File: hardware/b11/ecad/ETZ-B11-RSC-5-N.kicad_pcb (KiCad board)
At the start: 2 copper layers, 112.3 x 85.8 mm, 36 parts, among them SW1 MX-Hotswap-1U, SW10 MX-Hotswap-1U, SW11 MX-Hotswap-1U, SW12 MX-Hotswap-1U, SW13 MX-Hotswap-1U, SW14 MX-Hotswap-1U, SW15 MX-Hotswap-1U, SW16 MX-Hotswap-1U, SW17 MX-Hotswap-1U, SW18 MX-Hotswap-1U, SW2 MX-Hotswap-1U, SW3 MX-Hotswap-1U, SW4 MX-Hotswap-1U, SW5 MX-Hotswap-1U, SW6 MX-Hotswap-1U, SW7 MX-Hotswap-1U, SW8 MX-Hotswap-1U, SW9 MX-Hotswap-1U

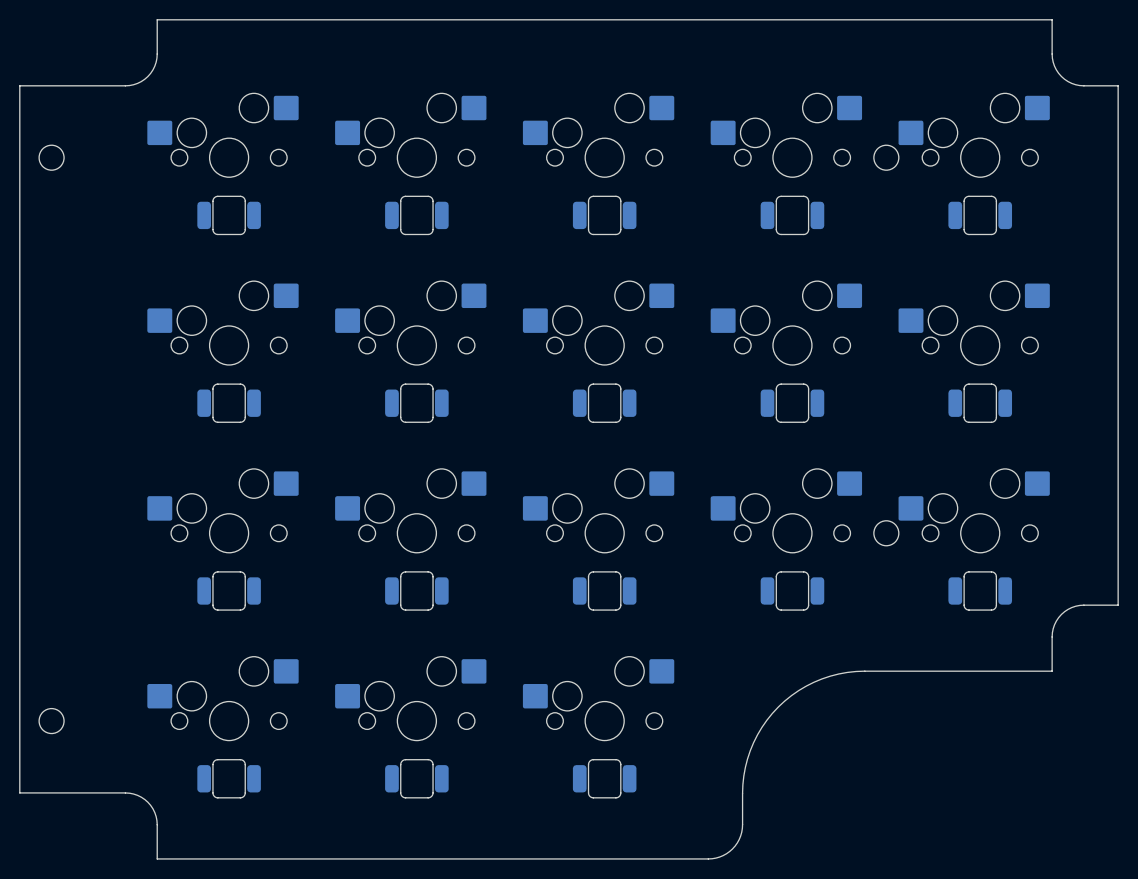
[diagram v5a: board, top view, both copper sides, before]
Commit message: fix(hardware/b11): adjust LED offset to 5.0mm and regenerate all carrier PCBs
Reduces south-facing LED offset from 5.9mm to 5.0mm (closer to the
standard 5.08mm switch-to-LED spacing). All 8 carrier PCBs regenerated.

Co-Authored-By: Claude Sonnet 4.6 <noreply@anthropic.com>
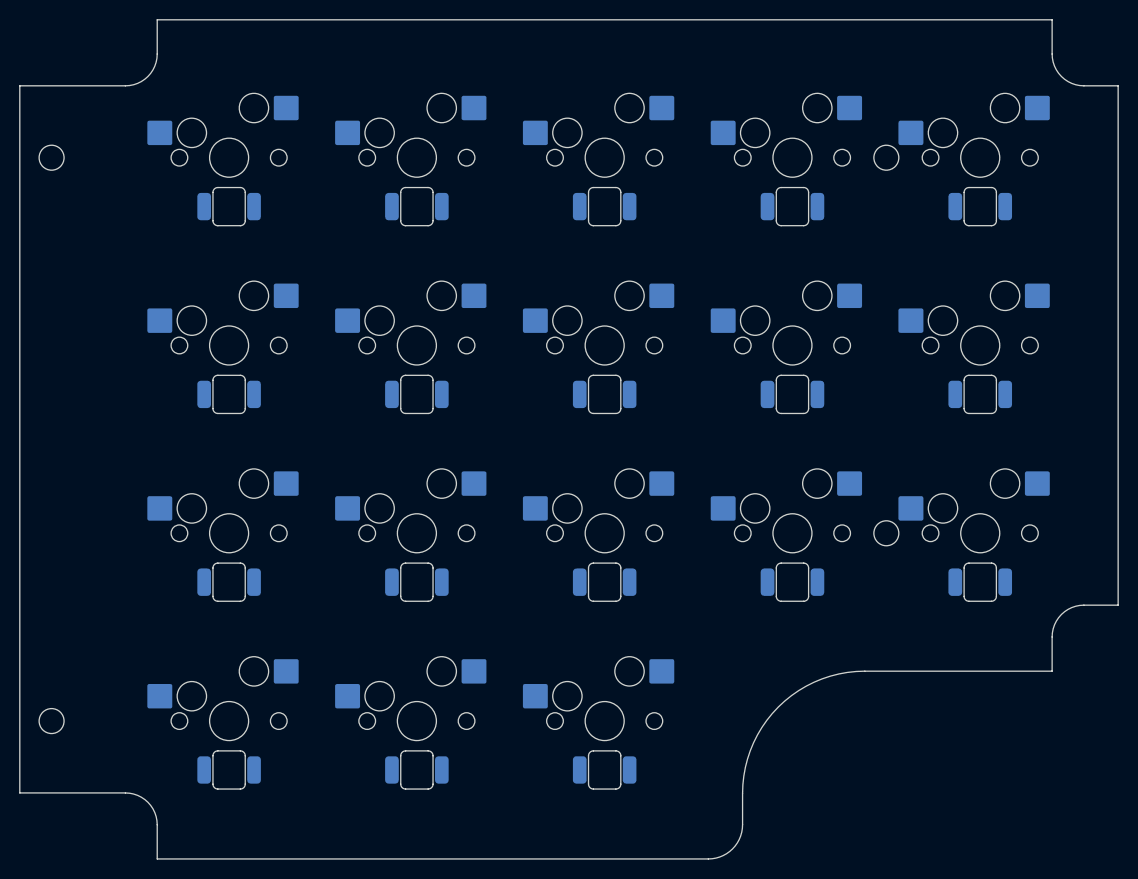
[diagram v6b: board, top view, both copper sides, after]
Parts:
- moved LED11 0.90 mm to (190.6, 116.7)
- moved LED12 0.90 mm to (171.3, 116.7)
- moved LED13 0.90 mm to (152.2, 116.7)
- moved LED14 0.90 mm to (132.9, 116.7)
- moved LED15 0.90 mm to (113.8, 116.7)
- moved LED1 0.90 mm to (190.6, 78.3)
- moved LED10 0.90 mm to (113.8, 97.5)
- moved LED16 0.90 mm to (152.2, 135.9)
- moved LED17 0.90 mm to (132.9, 135.9)
- moved LED18 0.90 mm to (113.8, 135.9)
- moved LED2 0.90 mm to (171.3, 78.3)
- moved LED3 0.90 mm to (152.2, 78.3)
- moved LED4 0.90 mm to (132.9, 78.3)
- moved LED5 0.90 mm to (113.8, 78.3)
- moved LED6 0.90 mm to (190.6, 97.5)
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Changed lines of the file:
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@@
 	(footprint "LED_SMD_6028_BackMount"
 		(layer "B.Cu")
-		(at 190.55 98.4)
+		(at 190.55 116.699999)
 		(descr "SMD 6028 back-paste reverse-mount LED, 5.88x2.80mm body, 3.20mm lens, slot 3.3x6.2mm")
 		(tags "LED SMD 6028 reverse-mount back-paste backlighting Choc")
-		(property "Reference" "LED6"
+		(property "Reference" "LED11"
 			(at 0 -2 0)
 			(layer "B.Fab")
@@
 	(footprint "LED_SMD_6028_BackMount"
 		(layer "B.Cu")
-		(at 132.95 98.4)
+		(at 132.95 97.5)
 		(descr "SMD 6028 back-paste reverse-mount LED, 5.88x2.80mm body, 3.20mm lens, slot 3.3x6.2mm")
 		(tags "LED SMD 6028 reverse-mount back-paste backlighting Choc")
@@
 	(footprint "LED_SMD_6028_BackMount"
 		(layer "B.Cu")
-		(at 132.95 117.6)
+		(at 152.15 116.699999)
 		(descr "SMD 6028 back-paste reverse-mount LED, 5.88x2.80mm body, 3.20mm lens, slot 3.3x6.2mm")
 		(tags "LED SMD 6028 reverse-mount back-paste backlighting Choc")
-		(property "Reference" "LED14"
+		(property "Reference" "LED13"
 			(at 0 -2 0)
 			(layer "B.Fab")
@@
 	(footprint "LED_SMD_6028_BackMount"
 		(layer "B.Cu")
-		(at 171.35 117.6)
+		(at 132.95 135.899999)
 		(descr "SMD 6028 back-paste reverse-mount LED, 5.88x2.80mm body, 3.20mm lens, slot 3.3x6.2mm")
 		(tags "LED SMD 6028 reverse-mount back-paste backlighting Choc")
-		(property "Reference" "LED12"
+		(property "Reference" "LED17"
 			(at 0 -2 0)
 			(layer "B.Fab")
@@
 	(footprint "LED_SMD_6028_BackMount"
 		(layer "B.Cu")
-		(at 152.15 79.2)
+		(at 171.35 78.3)
 		(descr "SMD 6028 back-paste reverse-mount LED, 5.88x2.80mm body, 3.20mm lens, slot 3.3x6.2mm")
 		(tags "LED SMD 6028 reverse-mount back-paste backlighting Choc")
-		(property "Reference" "LED3"
+		(property "Reference" "LED2"
 			(at 0 -2 0)
 			(layer "B.Fab")
@@
 	(footprint "LED_SMD_6028_BackMount"
 		(layer "B.Cu")
-		(at 152.15 136.799999)
+		(at 190.55 78.3)
 		(descr "SMD 6028 back-paste reverse-mount LED, 5.88x2.80mm body, 3.20mm lens, slot 3.3x6.2mm")
 		(tags "LED SMD 6028 reverse-mount back-paste backlighting Choc")
-		(property "Reference" "LED16"
+		(property "Reference" "LED1"
 			(at 0 -2 0)
 			(layer "B.Fab")
@@
 	(footprint "LED_SMD_6028_BackMount"
 		(layer "B.Cu")
-		(at 132.95 79.2)
+		(at 152.15 135.899999)
 		(descr "SMD 6028 back-paste reverse-mount LED, 5.88x2.80mm body, 3.20mm lens, slot 3.3x6.2mm")
 		(tags "LED SMD 6028 reverse-mount back-paste backlighting Choc")
-		(property "Reference" "LED4"
+		(property "Reference" "LED16"
 			(at 0 -2 0)
 			(layer "B.Fab")
@@
 	(footprint "LED_SMD_6028_BackMount"
 		(layer "B.Cu")
-		(at 113.75 117.6)
+		(at 152.15 78.3)
 		(descr "SMD 6028 back-paste reverse-mount LED, 5.88x2.80mm body, 3.20mm lens, slot 3.3x6.2mm")
 		(tags "LED SMD 6028 reverse-mount back-paste backlighting Choc")
-		(property "Reference" "LED15"
+		(property "Reference" "LED3"
 			(at 0 -2 0)
 			(layer "B.Fab")
@@
 	(footprint "LED_SMD_6028_BackMount"
 		(layer "B.Cu")
-		(at 132.95 136.799999)
+		(at 152.15 97.5)
 		(descr "SMD 6028 back-paste reverse-mount LED, 5.88x2.80mm body, 3.20mm lens, slot 3.3x6.2mm")
 		(tags "LED SMD 6028 reverse-mount back-paste backlighting Choc")
-		(property "Reference" "LED17"
+		(property "Reference" "LED8"
 			(at 0 -2 0)
 			(layer "B.Fab")
@@
 	(footprint "LED_SMD_6028_BackMount"
 		(layer "B.Cu")
-		(at 113.75 79.2)
+		(at 113.75 97.5)
 		(descr "SMD 6028 back-paste reverse-mount LED, 5.88x2.80mm body, 3.20mm lens, slot 3.3x6.2mm")
 		(tags "LED SMD 6028 reverse-mount back-paste backlighting Choc")
-		(property "Reference" "LED5"
+		(property "Reference" "LED10"
 			(at 0 -2 0)
 			(layer "B.Fab")
@@
 	(footprint "LED_SMD_6028_BackMount"
 		(layer "B.Cu")
-		(at 113.75 136.799999)
+		(at 171.35 97.5)
 		(descr "SMD 6028 back-paste reverse-mount LED, 5.88x2.80mm body, 3.20mm lens, slot 3.3x6.2mm")
 		(tags "LED SMD 6028 reverse-mount back-paste backlighting Choc")
-		(property "Reference" "LED18"
+		(property "Reference" "LED7"
 			(at 0 -2 0)
 			(layer "B.Fab")
@@
 	(footprint "LED_SMD_6028_BackMount"
 		(layer "B.Cu")
-		(at 152.15 98.4)
+		(at 113.75 78.3)
 		(descr "SMD 6028 back-paste reverse-mount LED, 5.88x2.80mm body, 3.20mm lens, slot 3.3x6.2mm")
 		(tags "LED SMD 6028 reverse-mount back-paste backlighting Choc")
-		(property "Reference" "LED8"
+		(property "Reference" "LED5"
 			(at 0 -2 0)
 			(layer "B.Fab")
@@
 	(footprint "LED_SMD_6028_BackMount"
 		(layer "B.Cu")
-		(at 113.75 98.4)
+		(at 132.95 78.3)
 		(descr "SMD 6028 back-paste reverse-mount LED, 5.88x2.80mm body, 3.20mm lens, slot 3.3x6.2mm")
 		(tags "LED SMD 6028 reverse-mount back-paste backlighting Choc")
-		(property "Reference" "LED10"
+		(property "Reference" "LED4"
 			(at 0 -2 0)
 			(layer "B.Fab")
@@
 	(footprint "LED_SMD_6028_BackMount"
 		(layer "B.Cu")
-		(at 171.35 98.4)
+		(at 190.55 97.5)
 		(descr "SMD 6028 back-paste reverse-mount LED, 5.88x2.80mm body, 3.20mm lens, slot 3.3x6.2mm")
 		(tags "LED SMD 6028 reverse-mount back-paste backlighting Choc")
-		(property "Reference" "LED7"
+		(property "Reference" "LED6"
 			(at 0 -2 0)
 			(layer "B.Fab")
@@
 	(footprint "LED_SMD_6028_BackMount"
 		(layer "B.Cu")
-		(at 190.55 117.6)
+		(at 113.75 135.899999)
 		(descr "SMD 6028 back-paste reverse-mount LED, 5.88x2.80mm body, 3.20mm lens, slot 3.3x6.2mm")
 		(tags "LED SMD 6028 reverse-mount back-paste backlighting Choc")
-		(property "Reference" "LED11"
+		(property "Reference" "LED18"
 			(at 0 -2 0)
 			(layer "B.Fab")
@@
 	(footprint "LED_SMD_6028_BackMount"
 		(layer "B.Cu")
-		(at 152.15 117.6)
+		(at 132.95 116.699999)
 		(descr "SMD 6028 back-paste reverse-mount LED, 5.88x2.80mm body, 3.20mm lens, slot 3.3x6.2mm")
 		(tags "LED SMD 6028 reverse-mount back-paste backlighting Choc")
-		(property "Reference" "LED13"
+		(property "Reference" "LED14"
 			(at 0 -2 0)
 			(layer "B.Fab")
@@
 	(footprint "LED_SMD_6028_BackMount"
 		(layer "B.Cu")
-		(at 171.35 79.2)
+		(at 171.35 116.699999)
 		(descr "SMD 6028 back-paste reverse-mount LED, 5.88x2.80mm body, 3.20mm lens, slot 3.3x6.2mm")
 		(tags "LED SMD 6028 reverse-mount back-paste backlighting Choc")
-		(property "Reference" "LED2"
+		(property "Reference" "LED12"
 			(at 0 -2 0)
 			(layer "B.Fab")
@@
 	(footprint "LED_SMD_6028_BackMount"
 		(layer "B.Cu")
-		(at 190.55 79.2)
+		(at 113.75 116.699999)
 		(descr "SMD 6028 back-paste reverse-mount LED, 5.88x2.80mm body, 3.20mm lens, slot 3.3x6.2mm")
 		(tags "LED SMD 6028 reverse-mount back-paste backlighting Choc")
-		(property "Reference" "LED1"
+		(property "Reference" "LED15"
 			(at 0 -2 0)
 			(layer "B.Fab")
